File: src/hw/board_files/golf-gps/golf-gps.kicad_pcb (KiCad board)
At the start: 4 copper layers, 62.2 x 91.7 mm, 63 parts, among them J1 USB_C_Receptacle_PowerOnly_6P, J3 Micro_SD_Card, SW1 SW_SPDT, SW2 RESET, SW3 BOOT, SW4 BTN_1, SW5 BTN_2, SW6 BTN_3, U1 MCP73831-2-OT, U2 TPS63031DSKR, U3 STM32L432KCU6, U4 NEO-M9N, Y1 32.768kHz

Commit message: PCB Progress
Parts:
- BT1: footprint Battery:BatteryHolder_Multicomp_BC-2001_1x2032 -> Battery:BatteryHolder_Keystone_3034_1x20mm; moved to F.Cu
- BT2, J1: moved to F.Cu
- J2: moved to B.Cu
- J3: footprint Connector_Card:microSD_HC_Molex_47219-2001 -> Connector_Card:microSD_HC_Wuerth_693072010801
- moved C15 148.4 mm to (145.0, 146.2)
- moved R12 145.6 mm to (154.6, 137.8), turned to 135 degrees
- moved C14 144.5 mm to (150.6, 124.5), turned to -90 degrees
- moved BT1 144.3 mm to (170.9, 122.7)
- moved R8 141.9 mm to (145.0, 147.8), turned to 180 degrees
- moved R13 139.9 mm to (153.9, 128.9), turned to 45 degrees
- moved R9 139.1 mm to (145.0, 144.6), turned to 180 degrees
- moved R14 137.5 mm to (152.8, 127.8), turned to 45 degrees
- moved R10 137.2 mm to (145.0, 143.0), turned to 180 degrees
- moved R15 132.1 mm to (148.0, 127.8), turned to 135 degrees
- moved SW3 129.8 mm to (119.7, 117.8)
- moved R11 123.3 mm to (141.6, 110.1)
- moved FB1 122.2 mm to (138.1, 110.4)
- moved C18 119.7 mm to (112.3, 126.0), turned to 90 degrees
- moved C20 119.4 mm to (112.3, 143.7), turned to 90 degrees
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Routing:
- net /Microcontroller/GPS_PPS: track 0.00 -> 19.6 mm, vias 0 -> 2
- net +3V3: track 12.3 -> 29.1 mm
- net /Microcontroller/GPS_TX: track 0.00 -> 14.1 mm, vias 0 -> 2
- net /Microcontroller/GPS_RX: track 0.00 -> 13.5 mm, vias 0 -> 2
- net /Microcontroller/SPI_SCK: track 0.00 -> 9.78 mm, vias 0 -> 1
- net /Microcontroller/SPI_MISO: track 0.00 -> 5.14 mm, vias 0 -> 2
- net /Power/V_USB: track 0.00 -> 4.99 mm
- net /Microcontroller/SPI_MOSI: track 0.00 -> 3.95 mm, vias 0 -> 2
- net /Microcontroller/BOOT: track 0.00 -> 3.19 mm
- net /Microcontroller/BTN_3: track 0.00 -> 3.04 mm
- net /Microcontroller/BTN_2: track 0.00 -> 3.01 mm
- net Net-(U3-PB3): track 0.00 -> 2.80 mm
- net /Microcontroller/BTN_1: track 0.00 -> 2.58 mm
- net Net-(D4-A): track 0.00 -> 1.93 mm
- net /Microcontroller/LCD_DC: track 0.00 -> 1.68 mm, vias 0 -> 1
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- removed copper zone on B.Cu, net /Power/V_USB
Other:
- board size 62.2 x 91.7 mm -> 71.6 x 91.7 mm
- board text added: "1"
- board text added: "2"
- board text added: "3"
- board text added: "RESET"

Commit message: PCB progress
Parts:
- moved SW2 43.7 mm to (119.7, 117.8), turned to -90 degrees
- moved C11 28.5 mm to (112.3, 126.0), turned to 90 degrees
- moved SW3 16.5 mm to (104.0, 123.2)
- moved C18 15.4 mm to (96.9, 126.3)
- moved C10 10.0 mm to (135.0, 128.8)
- moved FB1 1.50 mm to (139.1, 109.3), turned to 90 degrees
- moved R11 1.19 mm to (140.7, 109.3), turned to 90 degrees
- moved C22 0.90 mm to (128.2, 125.9)
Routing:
- net /Microcontroller/SPI_MISO: track 5.14 -> 26.9 mm, vias 2 -> 0
- net /Microcontroller/SPI_MOSI: track 3.95 -> 23.6 mm, vias 2 -> 0
- net /Microcontroller/SD_CS: track 0.00 -> 18.9 mm
- net GND: track 7.94 -> 22.6 mm, vias 14 -> 26
- net /Microcontroller/SPI_SCK: track 9.78 -> 0.00 mm, vias 1 -> 0
- net +3V3: track 29.1 -> 36.5 mm
- net Net-(U4-RF_IN): track 0.00 -> 6.99 mm
- net Net-(SW1-A): track 0.00 -> 6.30 mm
- net Net-(AE1-A): track 0.00 -> 6.11 mm
- net Net-(U4-~{RESET}): track 0.00 -> 4.18 mm
- net Net-(U4-VCC_RF): track 0.00 -> 3.76 mm
- net /Microcontroller/GPS_RX: track 13.5 -> 15.5 mm
- net /Microcontroller/LCD_DC: track 1.68 -> 0.00 mm, vias 1 -> 0
- added copper zone on In1.Cu, net GND
- added copper zone on In2.Cu, net GND
- removed copper zone on In1.Cu, net (none)
- removed copper zone on In2.Cu, net (none)
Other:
- board size 71.6 x 91.7 mm -> 71.6 x 92.1 mm

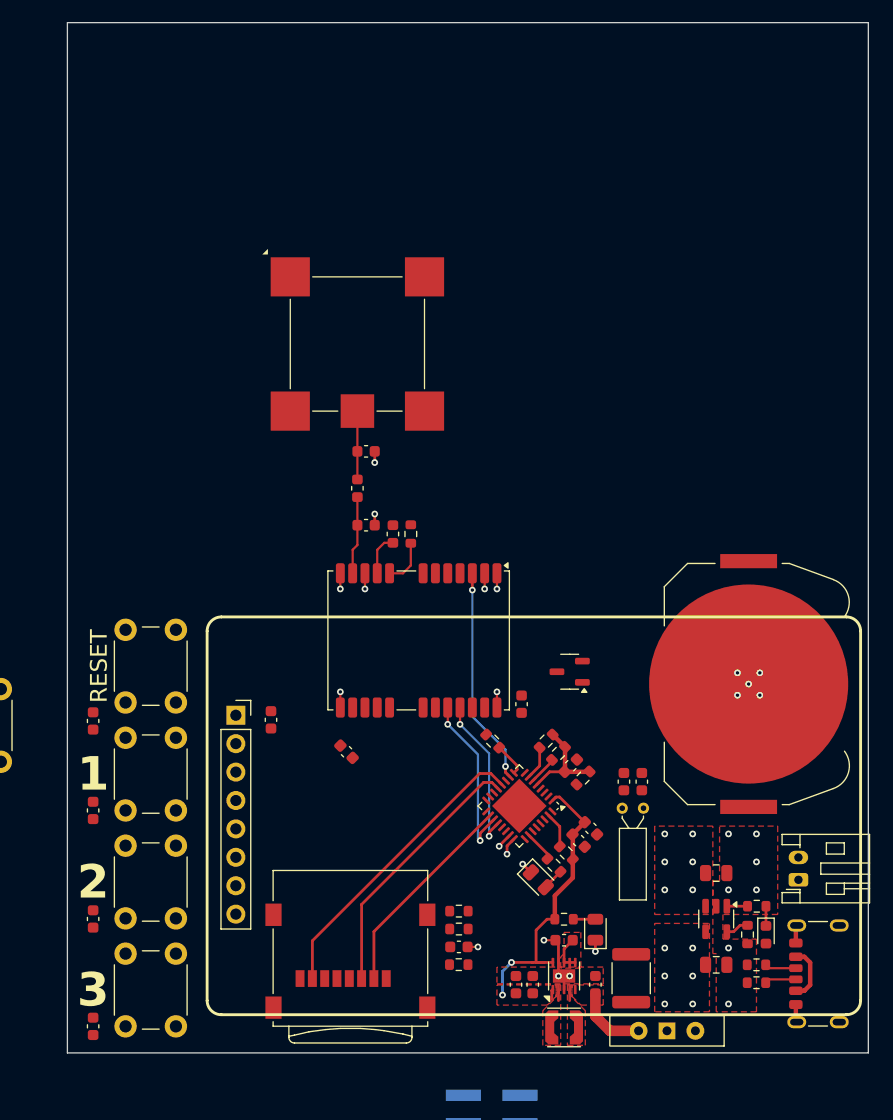
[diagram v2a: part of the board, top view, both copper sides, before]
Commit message: Added USBC to UART bridge for programming. Changed pinout. Added pinout spreadsheet in docs.
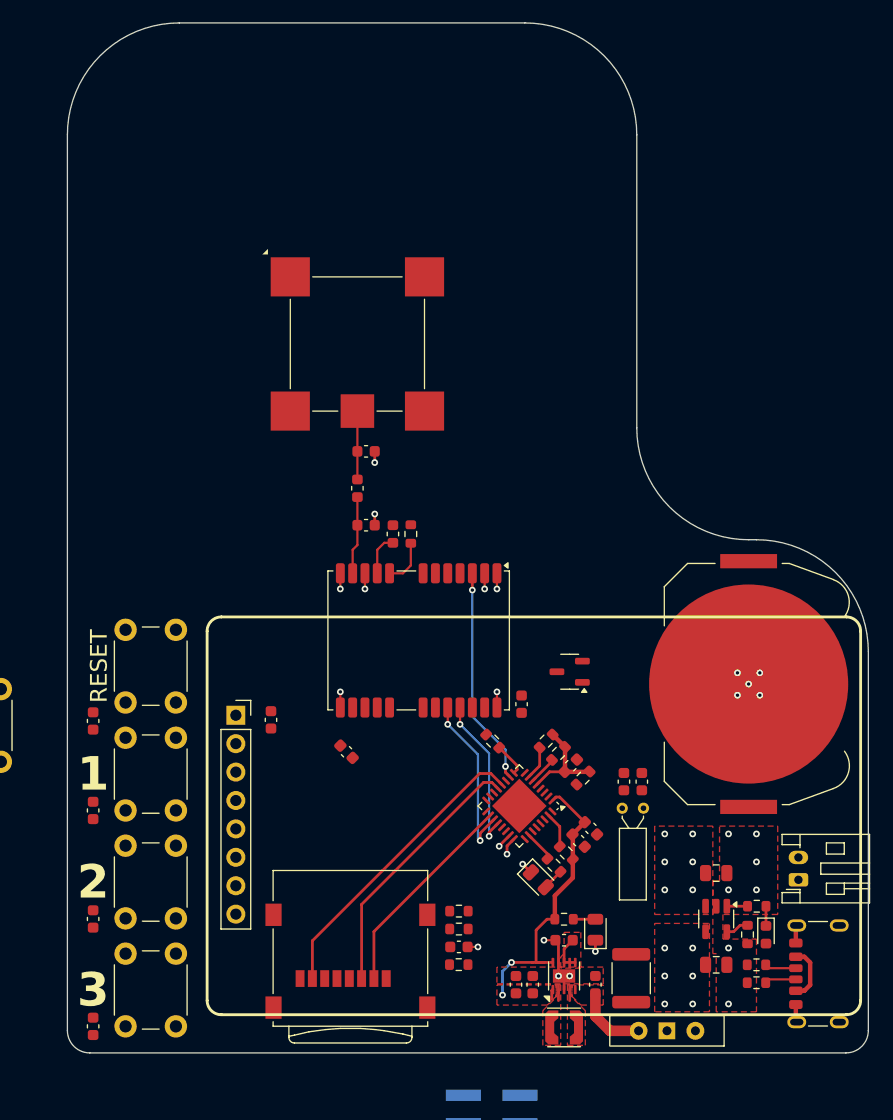
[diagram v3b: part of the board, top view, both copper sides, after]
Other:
- outline, holes or cut-outs redrawn
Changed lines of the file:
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@@
 		(layer "F.SilkS")
 	)
-	(gr_rect
-		(start 110 63.575)
-		(end 181.6 155.675)
+	(gr_arc
+		(start 170.9 109.8)
+		(mid 163.828932 106.871068)
+		(end 160.9 99.8)
 		(stroke
 			(width 0.05)
 			(type default)
 		)
-		(fill none)
+		(layer "Edge.Cuts")
+	)
+	(gr_line
+		(start 160.9 73.6)
+		(end 160.9 99.8)
+		(stroke
+			(width 0.05)
+			(type default)
+		)
+		(layer "Edge.Cuts")
+	)
+	(gr_arc
+		(start 171.6 109.8)
+		(mid 178.671068 112.728932)
+		(end 181.6 119.8)
+		(stroke
+			(width 0.05)
+			(type default)
+		)
+		(layer "Edge.Cuts")
+	)
+	(gr_arc
+		(start 150.9 63.6)
+		(mid 157.971068 66.528932)
+		(end 160.9 73.6)
+		(stroke
+			(width 0.05)
+			(type default)
+		)
+		(layer "Edge.Cuts")
+	)
+	(gr_line
+		(start 170.9 109.8)
+		(end 171.6 109.8)
+		(stroke
+			(width 0.05)
+			(type default)
+		)
+		(layer "Edge.Cuts")
+	)
+	(gr_arc
+		(start 112 155.675)
+		(mid 110.585786 155.089214)
+		(end 110 153.675)
+		(stroke
+			(width 0.05)
+			(type default)
+		)
+		(layer "Edge.Cuts")
+	)
+	(gr_arc
+		(start 181.6 153.675)
+		(mid 181.014214 155.089214)
+		(end 179.6 155.675)
+		(stroke
+			(width 0.05)
+			(type default)
+		)
+		(layer "Edge.Cuts")
+	)
+	(gr_line
+		(start 110 153.675)
+		(end 110 73.6)
+		(stroke
+			(width 0.05)
+			(type default)
+		)
+		(layer "Edge.Cuts")
+	)
+	(gr_line
+		(start 120 63.6)
+		(end 150.9 63.6)
+		(stroke
+			(width 0.05)
+			(type default)
+		)
+		(layer "Edge.Cuts")
+	)
+	(gr_arc
+		(start 110 73.6)
+		(mid 112.928932 66.528932)
+		(end 120 63.6)
+		(stroke
+			(width 0.05)
+			(type default)
+		)
+		(layer "Edge.Cuts")
+	)
+	(gr_line
+		(start 179.6 155.675)
+		(end 112 155.675)
+		(stroke
+			(width 0.05)
+			(type default)
+		)
+		(layer "Edge.Cuts")
+	)
+	(gr_line
+		(start 181.6 119.8)
+		(end 181.6 153.675)
+		(stroke
+			(width 0.05)
+			(type default)
+		)
 		(layer "Edge.Cuts")
 	)
@@
 	)
 	(zone
+		(net 3)
+		(net_name "GND")
+		(layer "F.Cu")
+		(hatch edge 0.5)
+		(priority 2)
+		(connect_pads
+			(clearance 0.5)
+		)
+		(min_thickness 0.25)
+		(filled_areas_thickness no)
+		(fill yes
+			(thermal_gap 0.5)
+			(thermal_bridge_width 0.5)
+			(island_removal_mode 1)
+			(island_area_min 10)
+		)
+		(polygon
+			(pts
+				(xy 157.9 149.5) (xy 157.9 148) (xy 148.4 148) (xy 148.4 149.5)
+			)
+		)
+	)
+	(zone
+		(net 4)
+		(net_name "VBAT")
+		(layer "F.Cu")
+		(hatch edge 0.5)
+		(priority 4)
+		(connect_pads
+			(clearance 0.5)
+		)
+		(min_thickness 0.25)
+		(filled_areas_thickness no)
+		(fill yes
+			(thermal_gap 0.5)
+			(thermal_bridge_width 0.5)
+			(island_removal_mode 1)
+			(island_area_min 10)
+		)
+		(polygon
+			(pts
+				(xy 167.7 143.3) (xy 167.7 135.4) (xy 162.5 135.4) (xy 162.5 143.3)
+			)
+		)
+	)
+	(zone
+		(net 8)
+		(net_name "Net-(U2-EN)")
+		(layer "F.Cu")
+		(hatch edge 0.5)
+		(priority 3)
+		(connect_pads
+			(clearance 0.5)
+		)
+		(min_thickness 0.25)
+		(filled_areas_thickness no)
+		(fill yes
+			(thermal_gap 0.5)
+			(thermal_bridge_width 0.5)
+			(island_removal_mode 1)
+			(island_area_min 10)
+		)
+		(polygon
+			(pts
+				(xy 154.4 144.9) (xy 155.9 144.9) (xy 155.9 148.1) (xy 154.1 148.1) (xy 154.1 147.1) (xy 154.4 146.8)
+			)
+		)
+	)
+	(zone
+		(net 6)
+		(net_name "+3V3")
+		(layer "F.Cu")
+		(hatch edge 0.5)
+		(priority 1)
+		(connect_pads
+			(clearance 0.5)
+		)
+		(min_thickness 0.25)
+		(filled_areas_thickness no)
+		(fill yes
+			(thermal_gap 0.5)
+			(thermal_bridge_width 0.5)
+			(island_removal_mode 1)
+			(island_area_min 10)
+		)
+		(polygon
+			(pts
+				(xy 153.7 149.6) (xy 153.7 150.6) (xy 152.9 151.4) (xy 148.4 151.4) (xy 148.4 149.6)
+			)
+		)
+	)
+	(zone
 		(net 12)
 		(net_name "Net-(U4-RF_IN)")
@@
 	)
 	(zone
-		(net 3)
-		(net_name "GND")
+		(net 5)
+		(net_name "/Power/V_USB")
 		(layer "F.Cu")
 		(hatch edge 0.5)
-		(priority 2)
+		(priority 4)
 		(connect_pads
 			(clearance 0.5)
@@
 		(polygon
 			(pts
-				(xy 157.9 149.5) (xy 157.9 148) (xy 148.4 148) (xy 148.4 149.5)
+				(xy 167.4 144.1) (xy 167.4 152) (xy 162.5 152) (xy 162.5 144.1)
 			)
 		)
 	)
 	(zone
-		(net 4)
-		(net_name "VBAT")
-		(layer "F.Cu")
+		(net 3)
+		(net_name "GND")
+		(layers "In1.Cu" "In2.Cu")
 		(hatch edge 0.5)
-		(priority 4)
+		(priority 6)
 		(connect_pads
 			(clearance 0.5)
@@
 		(polygon
 			(pts
-				(xy 167.7 143.3) (xy 167.7 135.4) (xy 162.5 135.4) (xy 162.5 143.3)
-			)
-		)
-	)
-	(zone
-		(net 8)
-		(net_name "Net-(U2-EN)")
-		(layer "F.Cu")
-		(hatch edge 0.5)
-		(priority 3)
-		(connect_pads
-			(clearance 0.5)
-		)
-		(min_thickness 0.25)
-		(filled_areas_thickness no)
-		(fill yes
-			(thermal_gap 0.5)
-			(thermal_bridge_width 0.5)
-			(island_removal_mode 1)
-			(island_area_min 10)
-		)
-		(polygon
-			(pts
-				(xy 154.4 144.9) (xy 155.9 144.9) (xy 155.9 148.1) (xy 154.1 148.1) (xy 154.1 147.1) (xy 154.4 146.8)
-			)
-		)
-	)
-	(zone
-		(net 6)
-		(net_name "+3V3")
-		(layer "F.Cu")
-		(hatch edge 0.5)
-		(priority 1)
-		(connect_pads
-			(clearance 0.5)
-		)
-		(min_thickness 0.25)
-		(filled_areas_thickness no)
-		(fill yes
-			(thermal_gap 0.5)
-			(thermal_bridge_width 0.5)
-			(island_removal_mode 1)
-			(island_area_min 10)
-		)
-		(polygon
-			(pts
-				(xy 153.7 149.6) (xy 153.7 150.6) (xy 152.9 151.4) (xy 148.4 151.4) (xy 148.4 149.6)
-			)
-		)
-	)
-	(zone
-		(net 5)
-		(net_name "/Power/V_USB")
-		(layer "F.Cu")
-		(hatch edge 0.5)
-		(priority 4)
-		(connect_pads
-			(clearance 0.5)
-		)
-		(min_thickness 0.25)
-		(filled_areas_thickness no)
-		(fill yes
-			(thermal_gap 0.5)
-			(thermal_bridge_width 0.5)
-			(island_removal_mode 1)
-			(island_area_min 10)
-		)
-		(polygon
-			(pts
-				(xy 167.4 144.1) (xy 167.4 152) (xy 162.5 152) (xy 162.5 144.1)
-			)
-		)
-	)
-	(zone
-		(net 3)
-		(net_name "GND")
-		(layers "In1.Cu" "In2.Cu")
-		(hatch edge 0.5)
-		(priority 6)
-		(connect_pads
-			(clearance 0.5)
-		)
-		(min_thickness 0.25)
-		(filled_areas_thickness no)
-		(fill yes
-			(thermal_gap 0.5)
-			(thermal_bridge_width 0.5)
-			(island_removal_mode 1)
-			(island_area_min 10)
-		)
-		(polygon
-			(pts
-				(xy 110.95 62) (xy 183.5 62) (xy 183.5 156.6) (xy 110.95 156.6)
-			)
-		)
+				(xy 86.65 43.9) (xy 204.4 43.9) (xy 204.4 173.9) (xy 86.65 173.9)
+			)
+		)
